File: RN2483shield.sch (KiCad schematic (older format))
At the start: 8 parts, among them J1 SCREW_TERMINAL, J2 SMA, J3 SMA, P1 CONN_01X06, P2 CONN_01X06, P3 CONN_01X06, U1 RN2483

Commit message: redraft of shield
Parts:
- removed J1: SCREW_TERMINAL, freetronics_footprints:SCREWTERMINAL-5MM-2, symbol SCREW_TERMINAL
- removed P1, P2, P3: CONN_01X06, Socket_Strips:Socket_Strip_Straight_1x06, symbol CONN_01X06
- added J1: LoRa_GPIO, symbol CONN_01X14
- added JP1, JP10, JP11, JP12, JP13, JP15, JP16, JP2, JP3, JP4, JP6, JP7, JP8, JP9: Jumper_NO_Small, symbol Jumper_NO_Small
- added JP14, JP5: Jumper_NC_Small, symbol Jumper_NC_Small
- added Q1, Q2: BSS138, symbol MOSFET_N
- added R1, R2, R3, R4, R5: 10k, symbol R
- J2, J3: footprint MyFootprints:SMA_BOARD_UPRIGHT -> (none)
- U1: value RN2483 -> RN2483/RN2903
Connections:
- net labels added: +3.3V, +5V, D0, D1, D2_RX, D3_TX, D4, D5, D6, D7, GPIO_0, GPIO_1, GPIO_10, GPIO_11, GPIO_12, GPIO_13, GPIO_2, GPIO_3, GPIO_4, GPIO_5, GPIO_6, GPIO_7, GPIO_8, GPIO_9, RX_RADIO, TX_RADIO
- net labels removed: 3.3VOLT, AD_P10, AD_P11, AD_P8, AD_P9, BATTERY, HW_RX, HW_TX, RN_RESET, UART_ARDUINO_TO_RADIO, UART_RADIO_TO_ARDUINO
- wire segments 15 -> 128
- no-connect marks 53 -> 32
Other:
- moved on the sheet: J2, J3, SHIELD1

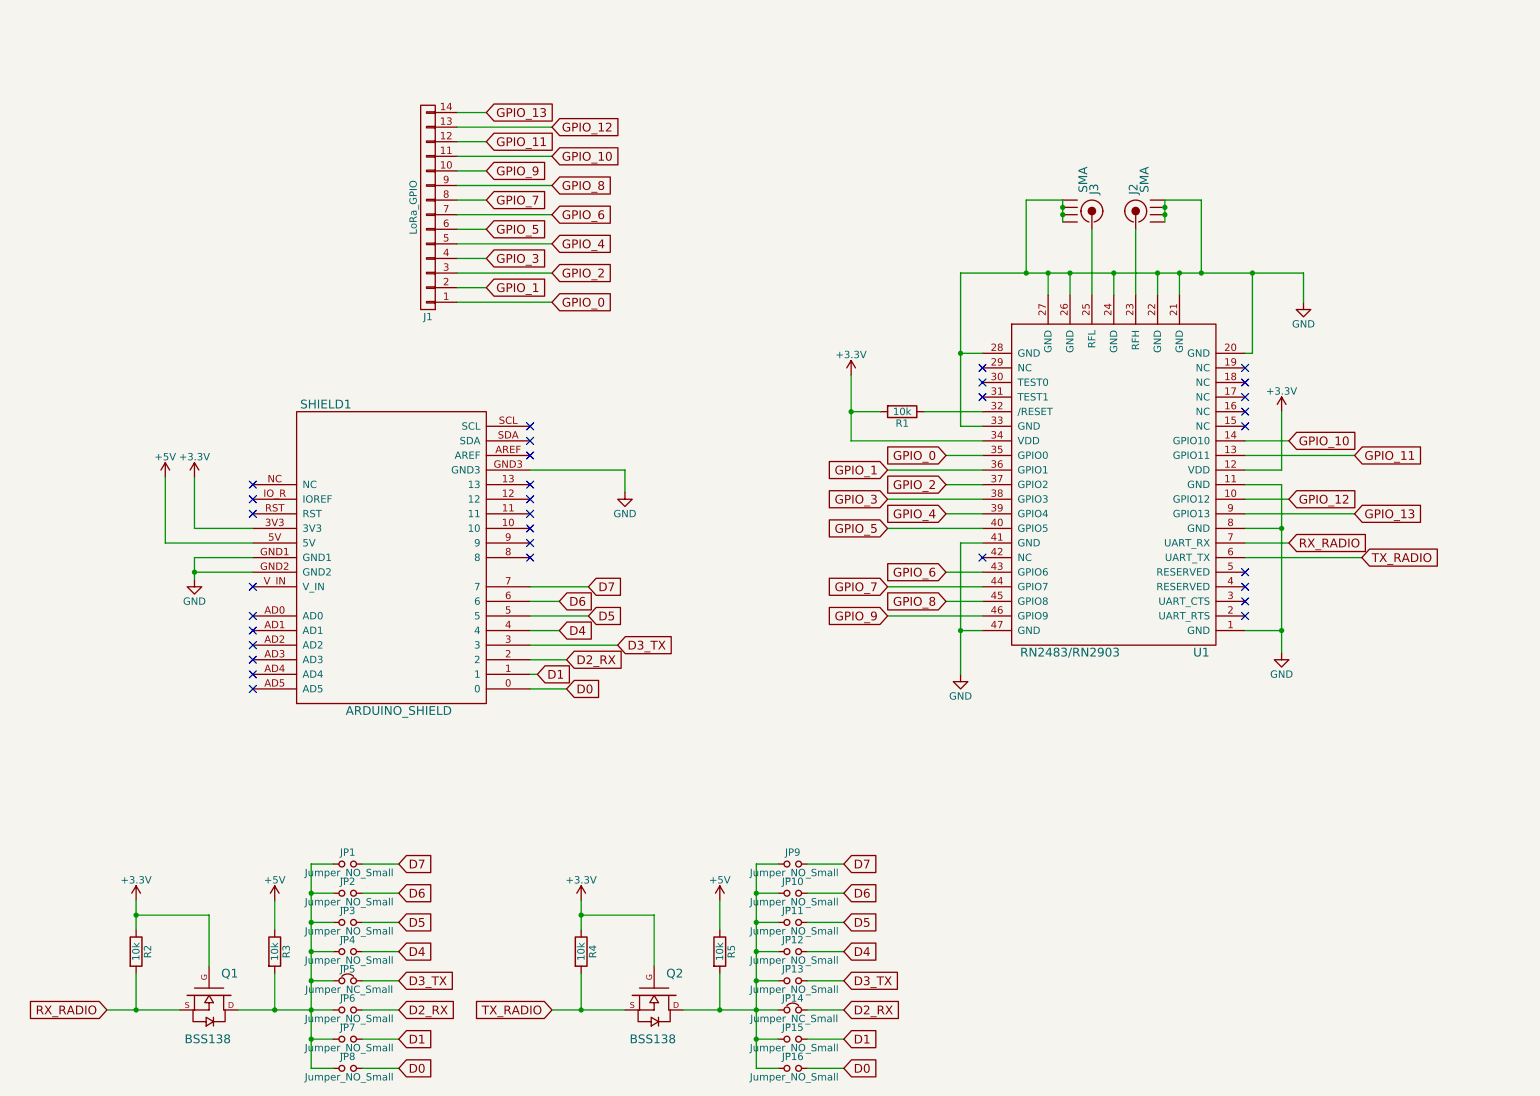
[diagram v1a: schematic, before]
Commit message: redrafted the board with edgeSMA, gpio breakouts and solderpad serial connections
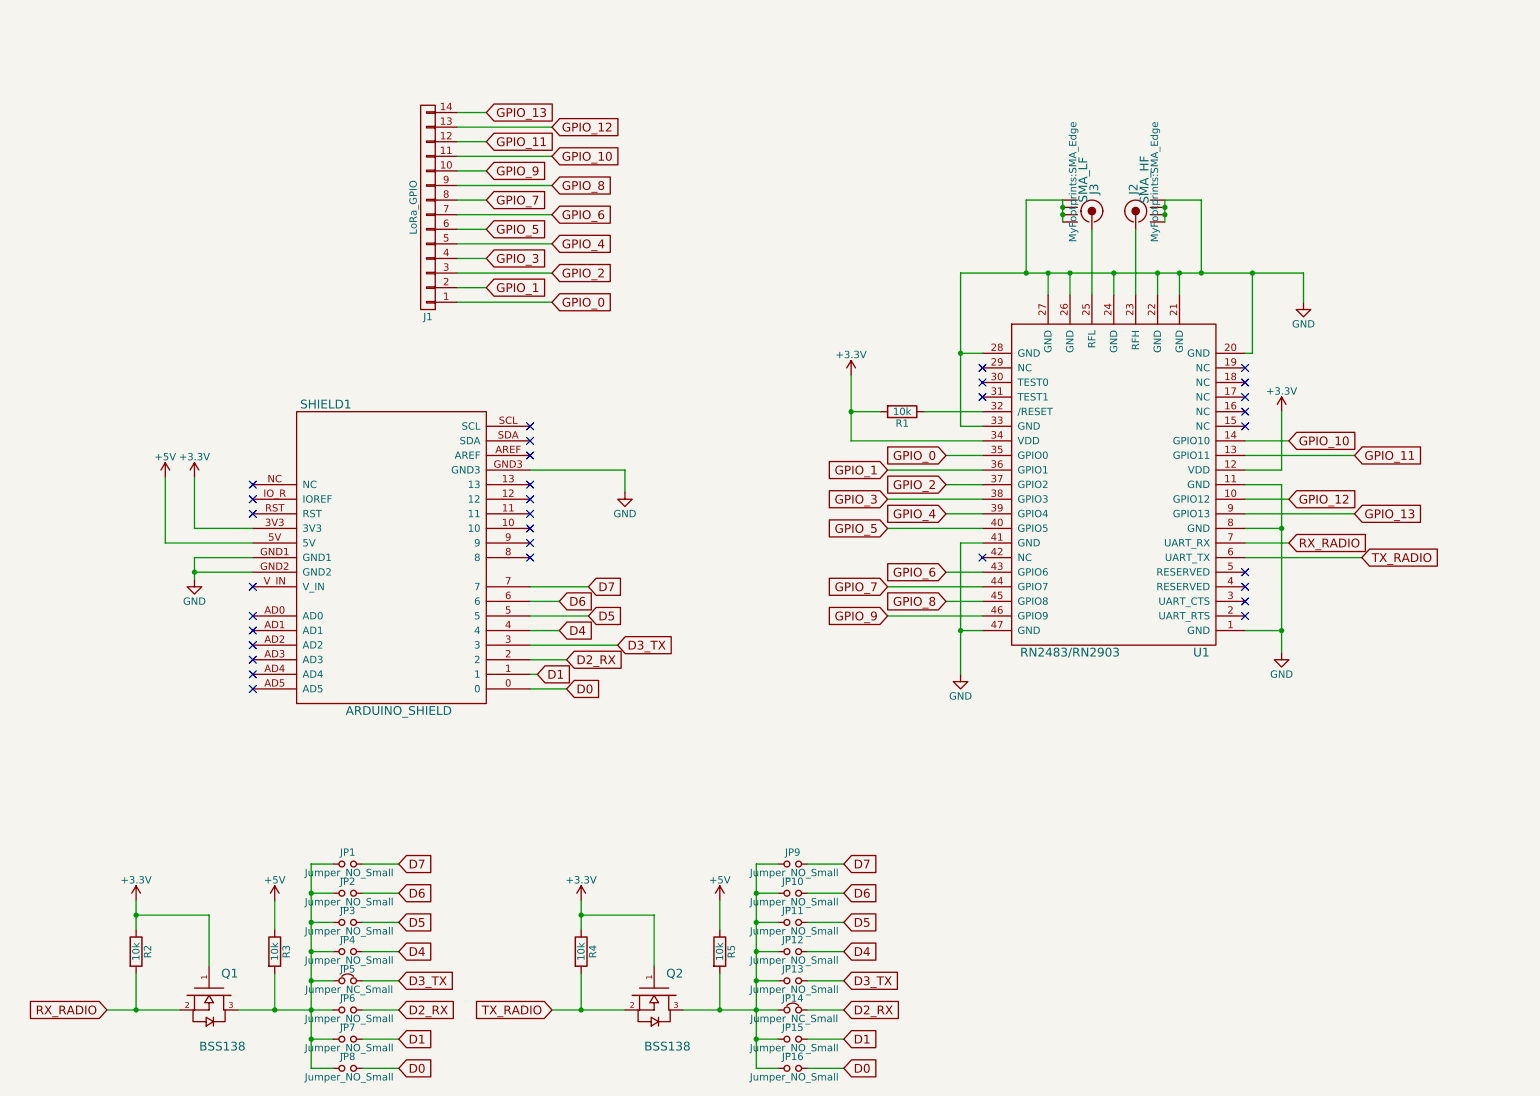
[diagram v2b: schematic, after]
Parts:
- removed Q1, Q2: BSS138, symbol MOSFET_N
- added Q1, Q2: BSS138, TO_SOT_Packages_SMD:SOT-23, symbol MOSFET_N_GSD
- J1: footprint (none) -> MyFootprints:CONN_1x14
- J2: value SMA -> SMA_HF; footprint (none) -> MyFootprints:SMA_Edge
- J3: value SMA -> SMA_LF; footprint (none) -> MyFootprints:SMA_Edge
- JP1, JP10, JP11, JP12, JP13, JP15, JP16, JP2, JP3, JP4, JP6, JP7, JP8, JP9: footprint (none) -> MyFootprints:NO_SMD_JPR
- JP14, JP5: footprint (none) -> MyFootprints:NC_SMD_JPR
- R1, R2, R3, R4, R5: footprint (none) -> Resistors_SMD:R_0603_HandSoldering
- SHIELD1: footprint freetronics_footprints:ARDUINO_SHIELD -> MyFootprints:ARDUINO_SHIELD_NOICSP
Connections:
- net +3V3: now also Q1.1 (G), Q2.1 (G)
- net RX_RADIO: now also Q1.2 (S)
- net TX_RADIO: now also Q2.2 (S)
- net at JP1.1, JP2.1, JP3.1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: now also Q1.3 (D)
- net at JP10.1, JP11.1, JP12.1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: now also Q2.3 (D)
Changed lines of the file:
@@
 NoConn ~ 2300 4800
 NoConn ~ 2300 4900
-$Comp
-L SMA J3
-U 1 1 569F8A06
-P 7750 1600
-F 0 "J3" H 7875 1915 60  0000 C CNN
-F 1 "SMA" H 7940 1840 60  0000 C CNN
-F 2 "" H 7925 1770 50  0000 C CNN
-F 3 "" H 7750 1600 60  0000 C CNN
-	1    7750 1600
-	0    1    -1   0
-$EndComp
 NoConn ~ 4200 3500
 NoConn ~ 2300 3700
@@
 F 0 "R1" V 6830 3000 50  0000 C CNN
 F 1 "10k" V 6750 3000 50  0000 C CNN
-F 2 "" V 6680 3000 50  0001 C CNN
+F 2 "Resistors_SMD:R_0603_HandSoldering" V 6680 3000 50  0001 C CNN
 F 3 "" H 6750 3000 50  0001 C CNN
 	1    6750 3000
@@
 F 0 "SHIELD1" H 2800 5250 60  0000 C CNN
 F 1 "ARDUINO_SHIELD" H 3300 3150 60  0000 C CNN
-F 2 "freetronics_footprints:ARDUINO_SHIELD" H 3250 3900 50  0001 C CNN
+F 2 "MyFootprints:ARDUINO_SHIELD_NOICSP" H 3250 3900 50  0001 C CNN
 F 3 "" H 3250 4100 60  0000 C CNN
 	1    3250 4100
@@
 Wire Wire Line
 	9100 4000 9900 4000
-$Comp
-L SMA J2
-U 1 1 56430378
-P 8650 1600
-F 0 "J2" H 8775 1915 60  0000 C CNN
-F 1 "SMA" H 8840 1840 60  0000 C CNN
-F 2 "" H 8825 1770 50  0000 C CNN
-F 3 "" H 8650 1600 60  0000 C CNN
-	1    8650 1600
-	0    -1   -1   0
-$EndComp
 Wire Wire Line
 	7600 1550 7600 2050
@@
 TX_RADIO
 $Comp
-L MOSFET_N Q1
-U 1 1 59344EFC
-P 2000 7000
-F 0 "Q1" V 1850 7200 60  0000 R CNN
-F 1 "BSS138" V 2300 7150 60  0000 R CNN
-F 2 "" H 2000 7000 60  0000 C CNN
-F 3 "" H 2000 7000 60  0000 C CNN
-	1    2000 7000
-	0    1    1    0
-$EndComp
-$Comp
 L R R2
 U 1 1 59344FB5
@@
 F 0 "R2" V 1580 6700 50  0000 C CNN
 F 1 "10k" V 1500 6700 50  0000 C CNN
-F 2 "" V 1430 6700 50  0001 C CNN
+F 2 "Resistors_SMD:R_0603_HandSoldering" V 1430 6700 50  0001 C CNN
 F 3 "" H 1500 6700 50  0001 C CNN
 	1    1500 6700
@@
 F 0 "R3" V 2530 6700 50  0000 C CNN
 F 1 "10k" V 2450 6700 50  0000 C CNN
-F 2 "" V 2380 6700 50  0001 C CNN
+F 2 "Resistors_SMD:R_0603_HandSoldering" V 2380 6700 50  0001 C CNN
 F 3 "" H 2450 6700 50  0001 C CNN
 	1    2450 6700
@@
 Connection ~ 2700 7300
 $Comp
-L MOSFET_N Q2
-U 1 1 5934798B
-P 5050 7000
-F 0 "Q2" V 4900 7200 60  0000 R CNN
-F 1 "BSS138" V 5350 7150 60  0000 R CNN
-F 2 "" H 5050 7000 60  0000 C CNN
-F 3 "" H 5050 7000 60  0000 C CNN
-	1    5050 7000
-	0    1    1    0
-$EndComp
-$Comp
 L R R4
 U 1 1 59347991
@@
 F 0 "R4" V 4630 6700 50  0000 C CNN
 F 1 "10k" V 4550 6700 50  0000 C CNN
-F 2 "" V 4480 6700 50  0001 C CNN
+F 2 "Resistors_SMD:R_0603_HandSoldering" V 4480 6700 50  0001 C CNN
 F 3 "" H 4550 6700 50  0001 C CNN
 	1    4550 6700
@@
 F 0 "R5" V 5580 6700 50  0000 C CNN
 F 1 "10k" V 5500 6700 50  0000 C CNN
-F 2 "" V 5430 6700 50  0001 C CNN
+F 2 "Resistors_SMD:R_0603_HandSoldering" V 5430 6700 50  0001 C CNN
 F 3 "" H 5500 6700 50  0001 C CNN
 	1    5500 6700
@@
 F 0 "JP1" H 2950 6180 50  0000 C CNN
 F 1 "Jumper_NO_Small" H 2960 6040 50  0000 C CNN
-F 2 "" H 2950 6100 50  0001 C CNN
+F 2 "MyFootprints:NO_SMD_JPR" H 2950 6100 50  0001 C CNN
 F 3 "" H 2950 6100 50  0001 C CNN
 	1    2950 6100
@@
 F 0 "JP2" H 2950 6380 50  0000 C CNN
 F 1 "Jumper_NO_Small" H 2960 6240 50  0000 C CNN
-F 2 "" H 2950 6300 50  0001 C CNN
+F 2 "MyFootprints:NO_SMD_JPR" H 2950 6300 50  0001 C CNN
 F 3 "" H 2950 6300 50  0001 C CNN
 	1    2950 6300
@@
 F 0 "JP3" H 2950 6580 50  0000 C CNN
 F 1 "Jumper_NO_Small" H 2960 6440 50  0000 C CNN
-F 2 "" H 2950 6500 50  0001 C CNN
+F 2 "MyFootprints:NO_SMD_JPR" H 2950 6500 50  0001 C CNN
 F 3 "" H 2950 6500 50  0001 C CNN
 	1    2950 6500
@@
 F 0 "JP4" H 2950 6780 50  0000 C CNN
 F 1 "Jumper_NO_Small" H 2960 6640 50  0000 C CNN
-F 2 "" H 2950 6700 50  0001 C CNN
+F 2 "MyFootprints:NO_SMD_JPR" H 2950 6700 50  0001 C CNN
 F 3 "" H 2950 6700 50  0001 C CNN
 	1    2950 6700
@@
 F 0 "JP6" H 2950 7180 50  0000 C CNN
 F 1 "Jumper_NO_Small" H 2960 7040 50  0000 C CNN
-F 2 "" H 2950 7100 50  0001 C CNN
+F 2 "MyFootprints:NO_SMD_JPR" H 2950 7100 50  0001 C CNN
 F 3 "" H 2950 7100 50  0001 C CNN
 	1    2950 7100
@@
 F 0 "JP7" H 2950 7380 50  0000 C CNN
 F 1 "Jumper_NO_Small" H 2960 7240 50  0000 C CNN
-F 2 "" H 2950 7300 50  0001 C CNN
+F 2 "MyFootprints:NO_SMD_JPR" H 2950 7300 50  0001 C CNN
 F 3 "" H 2950 7300 50  0001 C CNN
 	1    2950 7300
@@
 F 0 "JP8" H 2950 7580 50  0000 C CNN
 F 1 "Jumper_NO_Small" H 2960 7440 50  0000 C CNN
-F 2 "" H 2950 7500 50  0001 C CNN
+F 2 "MyFootprints:NO_SMD_JPR" H 2950 7500 50  0001 C CNN
 F 3 "" H 2950 7500 50  0001 C CNN
 	1    2950 7500
@@
 F 0 "JP9" H 6000 6180 50  0000 C CNN
 F 1 "Jumper_NO_Small" H 6010 6040 50  0000 C CNN
-F 2 "" H 6000 6100 50  0001 C CNN
+F 2 "MyFootprints:NO_SMD_JPR" H 6000 6100 50  0001 C CNN
 F 3 "" H 6000 6100 50  0001 C CNN
 	1    6000 6100
@@
 F 0 "JP10" H 6000 6380 50  0000 C CNN
 F 1 "Jumper_NO_Small" H 6010 6240 50  0000 C CNN
-F 2 "" H 6000 6300 50  0001 C CNN
+F 2 "MyFootprints:NO_SMD_JPR" H 6000 6300 50  0001 C CNN
 F 3 "" H 6000 6300 50  0001 C CNN
 	1    6000 6300
@@
 F 0 "JP11" H 6000 6580 50  0000 C CNN
 F 1 "Jumper_NO_Small" H 6010 6440 50  0000 C CNN
-F 2 "" H 6000 6500 50  0001 C CNN
+F 2 "MyFootprints:NO_SMD_JPR" H 6000 6500 50  0001 C CNN
 F 3 "" H 6000 6500 50  0001 C CNN
 	1    6000 6500
@@
 F 0 "JP12" H 6000 6780 50  0000 C CNN
 F 1 "Jumper_NO_Small" H 6010 6640 50  0000 C CNN
-F 2 "" H 6000 6700 50  0001 C CNN
+F 2 "MyFootprints:NO_SMD_JPR" H 6000 6700 50  0001 C CNN
 F 3 "" H 6000 6700 50  0001 C CNN
 	1    6000 6700
@@
 F 0 "JP13" H 6000 6980 50  0000 C CNN
 F 1 "Jumper_NO_Small" H 6010 6840 50  0000 C CNN
-F 2 "" H 6000 6900 50  0001 C CNN
+F 2 "MyFootprints:NO_SMD_JPR" H 6000 6900 50  0001 C CNN
 F 3 "" H 6000 6900 50  0001 C CNN
 	1    6000 6900
@@
 F 0 "JP15" H 6000 7380 50  0000 C CNN
 F 1 "Jumper_NO_Small" H 6010 7240 50  0000 C CNN
-F 2 "" H 6000 7300 50  0001 C CNN
+F 2 "MyFootprints:NO_SMD_JPR" H 6000 7300 50  0001 C CNN
 F 3 "" H 6000 7300 50  0001 C CNN
 	1    6000 7300
@@
 F 0 "JP16" H 6000 7580 50  0000 C CNN
 F 1 "Jumper_NO_Small" H 6010 7440 50  0000 C CNN
-F 2 "" H 6000 7500 50  0001 C CNN
+F 2 "MyFootprints:NO_SMD_JPR" H 6000 7500 50  0001 C CNN
 F 3 "" H 6000 7500 50  0001 C CNN
 	1    6000 7500
@@
 F 0 "JP5" H 2950 6980 50  0000 C CNN
 F 1 "Jumper_NC_Small" H 2960 6840 50  0000 C CNN
-F 2 "" H 2950 6900 50  0001 C CNN
+F 2 "MyFootprints:NC_SMD_JPR" H 2950 6900 50  0001 C CNN
 F 3 "" H 2950 6900 50  0001 C CNN
 	1    2950 6900
@@
 F 0 "JP14" H 6000 7180 50  0000 C CNN
 F 1 "Jumper_NC_Small" H 6010 7040 50  0000 C CNN
-F 2 "" H 6000 7100 50  0001 C CNN
+F 2 "MyFootprints:NC_SMD_JPR" H 6000 7100 50  0001 C CNN
 F 3 "" H 6000 7100 50  0001 C CNN
 	1    6000 7100
@@
 F 0 "J1" H 3500 2350 50  0000 C CNN
 F 1 "LoRa_GPIO" V 3600 1600 50  0000 C CNN
-F 2 "" H 3500 1600 50  0001 C CNN
+F 2 "MyFootprints:CONN_1x14" H 3500 1600 50  0001 C CNN
 F 3 "" H 3500 1600 50  0001 C CNN
 	1    3500 1600
@@
 Wire Wire Line
 	8350 1750 8350 2200
+$Comp
+L MOSFET_N_GSD Q2
+U 1 1 593593B2
+P 5050 7000
+F 0 "Q2" V 4900 7200 60  0000 R CNN
+F 1 "BSS138" V 5400 7250 60  0000 R CNN
+F 2 "TO_SOT_Packages_SMD:SOT-23" H 5050 7000 60  0001 C CNN
+F 3 "" H 5050 7000 60  0000 C CNN
+	1    5050 7000
+	0    1    1    0
+$EndComp
+$Comp
+L MOSFET_N_GSD Q1
+U 1 1 5935973E
+P 2000 7000
+F 0 "Q1" V 1850 7200 60  0000 R CNN
+F 1 "BSS138" V 2350 7250 60  0000 R CNN
+F 2 "TO_SOT_Packages_SMD:SOT-23" H 2000 7000 60  0001 C CNN
+F 3 "" H 2000 7000 60  0000 C CNN
+	1    2000 7000
+	0    1    1    0
+$EndComp
+$Comp
+L SMA J2
+U 1 1 5935A93C
+P 8650 1600
+F 0 "J2" H 8775 1915 60  0000 C CNN
+F 1 "SMA_HF" H 8840 1840 60  0000 C CNN
+F 2 "MyFootprints:SMA_Edge" H 8825 1770 50  0000 C CNN
+F 3 "" H 8650 1600 60  0000 C CNN
+	1    8650 1600
+	0    -1   -1   0
+$EndComp
+$Comp
+L SMA J3
+U 1 1 5935A9DA
+P 7750 1600
+F 0 "J3" H 7875 1915 60  0000 C CNN
+F 1 "SMA_LF" H 7940 1840 60  0000 C CNN
+F 2 "MyFootprints:SMA_Edge" H 7925 1770 50  0000 C CNN
+F 3 "" H 7750 1600 60  0000 C CNN
+	1    7750 1600
+	0    1    -1   0
+$EndComp
 $EndSCHEMATC
